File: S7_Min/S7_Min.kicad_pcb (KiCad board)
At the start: 4 copper layers, 78 x 72 mm, 160 parts, among them J1 Barrel_Jack_Switch, J2 XILINX_JTAG, J3 HDMI_A, J4 Conn_02x12_Odd_Even, Q1 DMN2020L, Q2 DMN63D8LDW, Q3 DMN63D8LDW, Q4 DMN63D8LDW, Q5 DMN2020L, U1 TPS65581, U2 XC7S50-FTGB196, U3 REF3012, U4 QSPI_Flash_SOIC8, U5 MT47H128M16XX, U6 AZ1117-5.0, U7 TPD12S521, X1 DSC61XX

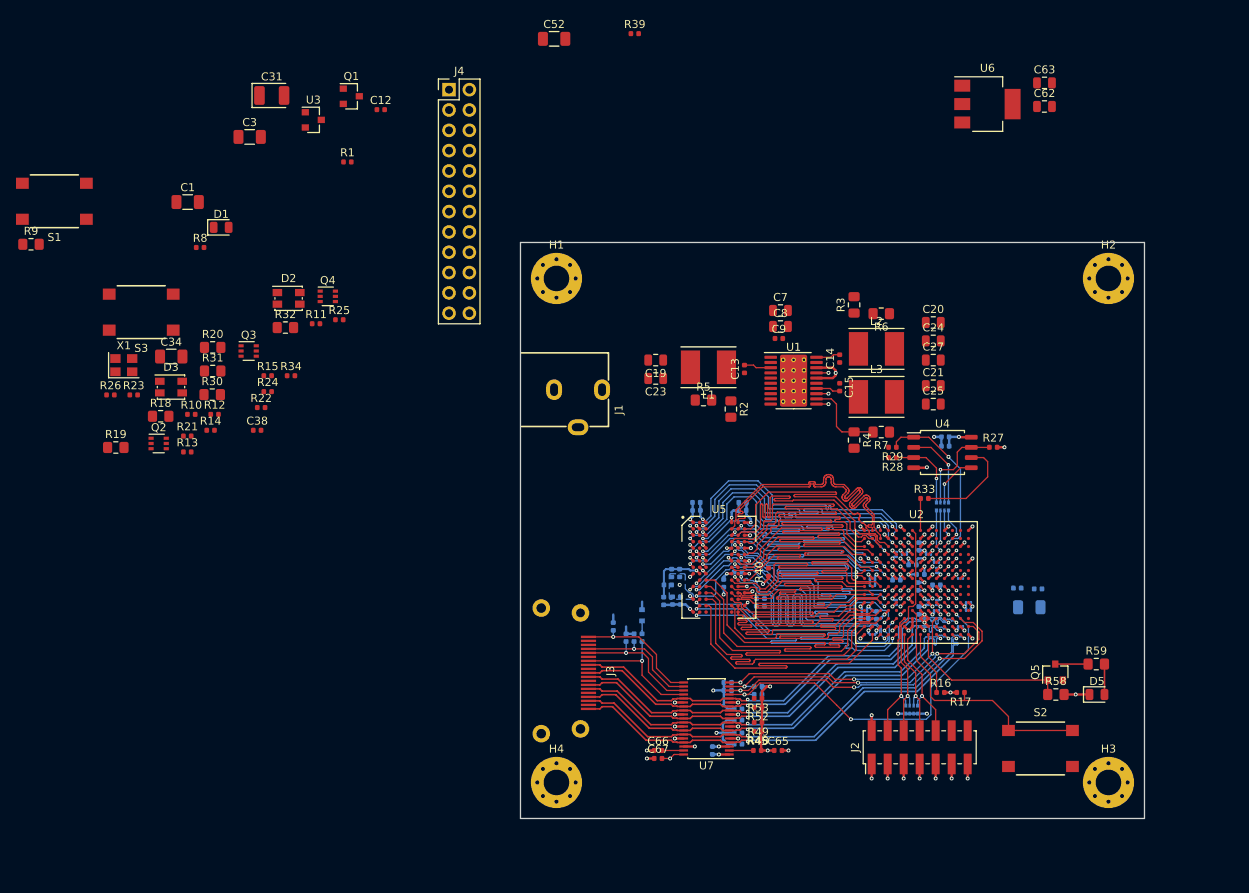
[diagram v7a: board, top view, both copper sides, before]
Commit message: Layout is completed, DRC passed, first pass on a silk layers
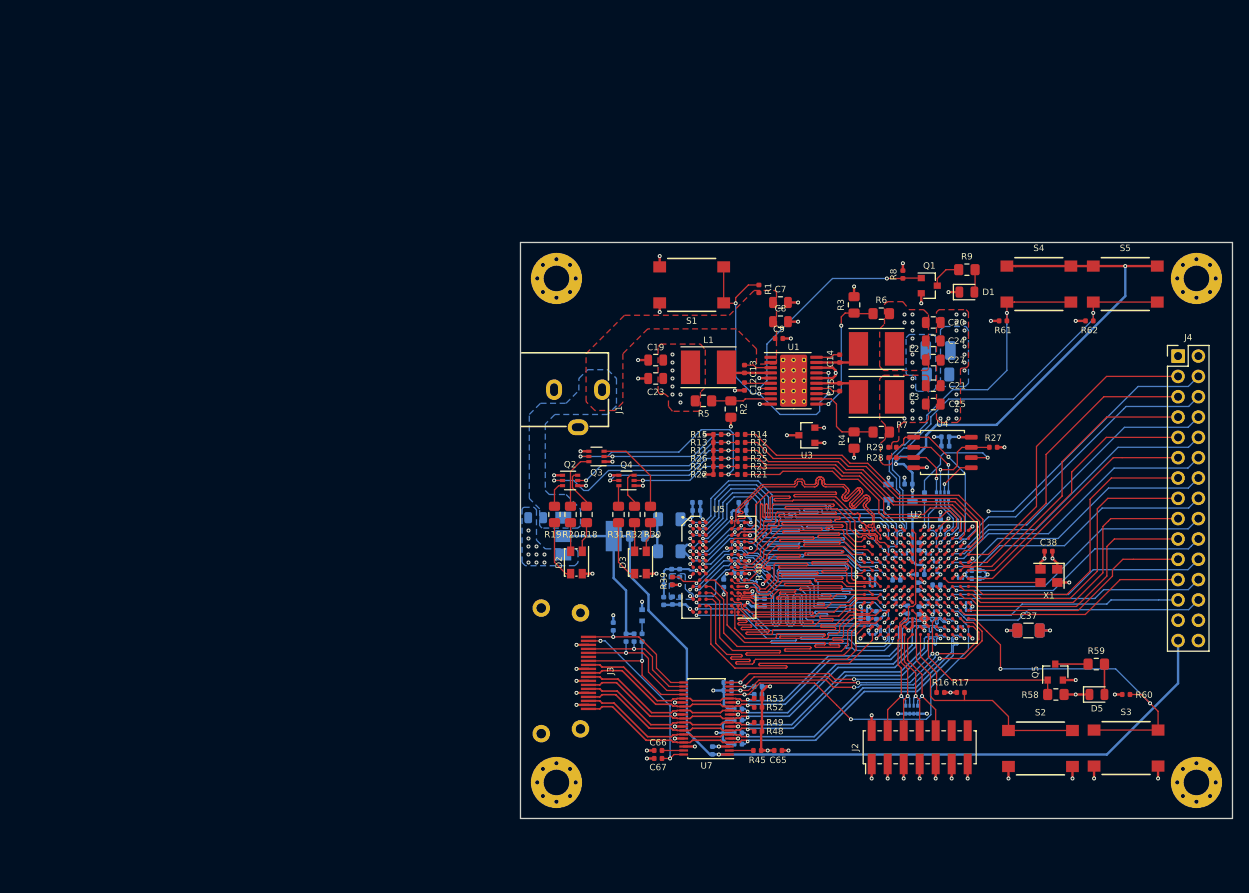
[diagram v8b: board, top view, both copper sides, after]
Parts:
- added C68: 4.7 uF, Capacitor_SMD:C_0402_1005Metric, B.Cu at (139.5, 82.2)
- added C69: 0.47 uF, my_parts:C_0201_0603Metric, B.Cu at (141.0, 92.0)
- added FB1: 600R, Inductors_SMD:L_0805, B.Cu at (140.0, 85.2)
- added FB2: 600R, Inductors_SMD:L_0805, B.Cu at (137.0, 83.2)
- added R60: 4.75K, Resistor_SMD:R_0402_1005Metric, F.Cu at (166.7, 108.5)
- added R61: 4.75K, Resistor_SMD:R_0402_1005Metric, F.Cu at (151.3, 61.8)
- added R62: 4.75K, Resistor_SMD:R_0402_1005Metric, F.Cu at (162.1, 61.8)
- added S4: USER_1, my_parts:B3FS_1010P, F.Cu at (155.8, 57.2)
- added S5: USER_2, my_parts:B3FS_1010P, F.Cu at (166.6, 57.2)
- C1, C3, C31, C34, C52, C62, C63, R33, R34, U6: moved to B.Cu
- C37: moved to F.Cu
- J4: value Conn_02x12_Odd_Even -> Conn_02x15_Odd_Even; footprint Connector_PinHeader_2.54mm:PinHeader_2x12_P2.54mm_Vertical -> Connector_PinHeader_2.54mm:PinHeader_2x15_P2.54mm_Vertical
- moved S3 134.6 mm to (166.7, 115.2), turned to 180 degrees
- moved X1 118.6 mm to (157.1, 93.7), turned to 180 degrees
- moved R9 117.0 mm to (146.8, 55.4)
- moved C34 112.5 mm to (154.5, 100.5)
- moved C38 100.1 mm to (157.0, 90.6), turned to 180 degrees
- moved J4 97.0 mm to (173.2, 66.2)
- moved D1 93.6 mm to (146.8, 58.2)
- moved C3 91.0 mm to (143.2, 68.5)
- moved C31 89.2 mm to (143.2, 65.5)
- moved R8 87.9 mm to (138.8, 56.0), turned to 90 degrees
- moved R34 83.3 mm to (143.5, 87.1), turned to 270 degrees
- moved C62 81.8 mm to (92.9, 86.4)
- moved S1 80.3 mm to (112.4, 57.3)
- moved R23 76.5 mm to (118.6, 80.0)
- moved R26 76.3 mm to (115.6, 79.0), turned to 180 degrees
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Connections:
- net Net-(R34-Pad2) renamed /Bank0_14/FPGA_PUDC
- J4 pad 1: Net-(J4-Pad1) -> +3V3
- J4 pad 10: Net-(J4-Pad10) -> GPIO_7
- J4 pad 11: Net-(J4-Pad11) -> GPIO_8
- J4 pad 12: Net-(J4-Pad12) -> GPIO_9
- J4 pad 13: Net-(J4-Pad13) -> GPIO_10
- J4 pad 14: Net-(J4-Pad14) -> GPIO_11
- J4 pad 15: Net-(J4-Pad15) -> GPIO_12
- J4 pad 16: Net-(J4-Pad16) -> GPIO_13
- J4 pad 17: Net-(J4-Pad17) -> GPIO_14
- J4 pad 18: Net-(J4-Pad18) -> GPIO_15
- J4 pad 19: Net-(J4-Pad19) -> GPIO_16
- J4 pad 2: Net-(J4-Pad2) -> GND
- J4 pad 20: Net-(J4-Pad20) -> GPIO_17
- J4 pad 21: Net-(J4-Pad21) -> GPIO_18
- J4 pad 22: Net-(J4-Pad22) -> GPIO_19
- J4 pad 23: Net-(J4-Pad23) -> GPIO_20
- J4 pad 24: Net-(J4-Pad24) -> GPIO_21
- J4 pad 3: Net-(J4-Pad3) -> GPIO_0
- J4 pad 4: Net-(J4-Pad4) -> GPIO_1
- J4 pad 5: Net-(J4-Pad5) -> GPIO_2
- J4 pad 6: Net-(J4-Pad6) -> GPIO_3
- J4 pad 7: Net-(J4-Pad7) -> GPIO_4
- J4 pad 8: Net-(J4-Pad8) -> GPIO_5
- J4 pad 9: Net-(J4-Pad9) -> GPIO_6
- U2 pad A10: Net-(U2-PadA10) -> GPIO_1
- U2 pad A12: Net-(U2-PadA12) -> /Bank0_14/RGB2_R
- U2 pad A13: Net-(U2-PadA13) -> /Bank0_14/RGB2_G
- U2 pad B13: Net-(U2-PadB13) -> /Bank0_14/RGB2_B
- U2 pad B14: Net-(U2-PadB14) -> /Bank0_14/RGB1_R
- U2 pad B6: Net-(U2-PadB6) -> /Bank34/USER_2
- U2 pad C12: Net-(U2-PadC12) -> GPIO_3
- U2 pad C14: Net-(U2-PadC14) -> /Bank0_14/RGB1_G
- U2 pad D12: Net-(U2-PadD12) -> GPIO_5
- U2 pad D13: Net-(U2-PadD13) -> /Bank0_14/RGB1_B
- U2 pad D14: Net-(U2-PadD14) -> GPIO_0
- U2 pad E11: Net-(U2-PadE11) -> GPIO_7
- U2 pad E12: Net-(U2-PadE12) -> GPIO_9
- U2 pad E13: Net-(U2-PadE13) -> GPIO_2
- U2 pad E4: Net-(U2-PadE4) -> /Bank34/USER_1
- U2 pad F11: Net-(U2-PadF11) -> GPIO_11
- U2 pad F12: Net-(U2-PadF12) -> GPIO_13
- U2 pad F13: Net-(U2-PadF13) -> GPIO_4
- U2 pad F14: Net-(U2-PadF14) -> GPIO_6
- U2 pad G14: Net-(U2-PadG14) -> GPIO_8
- U2 pad H11: Net-(U2-PadH11) -> GPIO_15
- U2 pad H12: Net-(U2-PadH12) -> GPIO_17
- U2 pad H13: /Bank0_14/SYSRESET -> GPIO_12
- U2 pad H14: Net-(U2-PadH14) -> GPIO_10
- U2 pad J11: /Bank0_14/RGB2_G -> GPIO_19
- U2 pad J12: /Bank0_14/RGB2_B -> GPIO_21
- U2 pad J13: /Bank0_14/RGB1_R -> GPIO_16
- U2 pad J14: /Bank0_14/RGB1_G -> GPIO_14
- U2 pad K11: /Bank0_14/RGB1_B -> GPIO_23
- U2 pad K12: Net-(U2-PadK12) -> GPIO_22
- U2 pad L13: /Bank0_14/RGB2_R -> GPIO_20
- U2 pad L14: Net-(U2-PadL14) -> GPIO_18
- U2 pad M14: Net-(U2-PadM14) -> /Bank0_14/SYSRESET
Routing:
- net +5V: track 4.02 -> 122.5 mm
- net +1V8: track 31.1 -> 104.4 mm, vias 23 -> 34
- net GND: track 111.3 -> 179.3 mm, vias 91 -> 160
- net /Bank34/USER_2: track 0.00 -> 55.2 mm, vias 0 -> 2
- net /Bank34/USER_1: track 0.00 -> 53.0 mm, vias 0 -> 2
- net /Bank0_14/SYSRESET: track 0.00 -> 43.6 mm, vias 0 -> 2
- net GPIO_1: track 0.00 -> 40.7 mm, vias 0 -> 2
- net GPIO_0: track 0.00 -> 39.8 mm
- net GPIO_2: track 0.00 -> 39.7 mm
- net /Bank0_14/RGB1_B: track 0.71 -> 40.1 mm, vias 1 -> 0
- net Net-(R1-Pad1): track 3.00 -> 41.8 mm, vias 2 -> 4
- net GPIO_3: track 0.00 -> 38.5 mm, vias 0 -> 1
- net GPIO_7: track 0.00 -> 38.2 mm, vias 0 -> 1
- net GPIO_10: track 0.00 -> 37.9 mm
- net GPIO_5: track 0.00 -> 37.9 mm, vias 0 -> 1
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- added copper zone on B.Cu, net +12V
- added copper zone on F.Cu, net +12V
- added copper zone on B.Cu, net +1V0
- added copper zone on F.Cu, net +1V0
- added copper zone on In2.Cu, net +1V0
- added copper zone on F.Cu, net +1V8
- added copper zone on In2.Cu, net +1V8
- added copper zone on F.Cu, net +3V3
- added copper zone on In2.Cu, net +3V3
- added copper zone on F.Cu, net GND
- added copper zone on In1.Cu, net GND
- added copper zone on In1.Cu, net GNDA
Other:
- board size 78 x 72 mm -> 89 x 72 mm
